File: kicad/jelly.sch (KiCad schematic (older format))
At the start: 1 part

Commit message: Add some components
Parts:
- added BT1: BATTERY, battery_custom, symbol BATTERY
- added D1, D2: LED, KiCad/LEDs.pretty:LED-5MM, symbol LED-RESCUE-bristle_bot
- added M1, M2: PAGER_MOTOR, footprints:pager_motor_custom, symbol Pager_motor
- added P1, P2, P3, P4, P5, P6, P7, P8: CONN_01X01, KiCad/Pin_Headers.pretty:Pin_Header_Straight_1x01, symbol CONN_01X01
- added Q1, Q2: 2N7000, KiCad/TO_SOT_Packages_THT.pretty:TO-92_Rugged, symbol 2N7000
- added R1, R3: 220, KiCad/Discret.pretty:R1, symbol R-RESCUE-bristle_bot
- added R2, R4: R, KiCad/Discret.pretty:R3-5, symbol R-RESCUE-bristle_bot
- added RV1: DUAL_POT, symbol DUAL_POT
- added SW1: SWITCH_INV, switch_small_custom, symbol SWITCH_INV
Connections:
- new net: BT1.1 (+), SW1.1
- new net: Q1.2 (G), R1.2, RV1.4
- new net: Q2.2 (G), R3.2, RV1.1
- new net: D2.2 (K), R4.2
- new net: D1.2 (K), R2.2
- new net GND: BT1.2 (-), Q1.1 (S), Q2.1 (S), RV1.2, RV1.5
- new net VCC: D1.1 (A), D2.1 (A), M1.1 (+), M2.1 (+), P1.1 (P1), P2.1 (P1), P7.1 (P1), P8.1 (P1), R1.1, R3.1, SW1.2
- new net Vout1: M1.2 (-), P3.1 (P1), P5.1 (P1), Q1.3 (D), R2.1
- new net Vout2: M2.2 (-), P4.1 (P1), P6.1 (P1), Q2.3 (D), R4.1

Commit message: Play with layout
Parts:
- BT1: footprint battery_custom -> (none)
- SW1: footprint switch_small_custom -> (none)
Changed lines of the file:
@@
 F 0 "BT1" H 5550 6200 50  0000 C CNN
 F 1 "BATTERY" H 5550 5810 50  0000 C CNN
-F 2 "battery_custom" H 5550 6000 60  0000 C CNN
+F 2 "" H 5550 6000 60  0000 C CNN
 F 3 "~" H 5550 6000 60  0000 C CNN
 	1    5550 6000
@@
 $EndComp
 $Comp
-L GND-RESCUE-bristle_bot #PWR3
+L GND-RESCUE-bristle_bot #PWR01
 U 1 1 57C0D38E
 P 6000 6000
-F 0 "#PWR3" H 6000 6000 30  0001 C CNN
+F 0 "#PWR01" H 6000 6000 30  0001 C CNN
 F 1 "GND" H 6000 5930 30  0001 C CNN
 F 2 "" H 6000 6000 60  0000 C CNN
@@
 $EndComp
 $Comp
-L VCC #PWR1
+L VCC #PWR02
 U 1 1 57C0D391
 P 3900 6100
-F 0 "#PWR1" H 3900 6200 30  0001 C CNN
+F 0 "#PWR02" H 3900 6200 30  0001 C CNN
 F 1 "VCC" H 3900 6200 30  0000 C CNN
 F 2 "" H 3900 6100 60  0000 C CNN
@@
 $EndComp
 $Comp
-L VCC #PWR2
+L VCC #PWR03
 U 1 1 57C0D393
 P 5300 2800
-F 0 "#PWR2" H 5300 2900 30  0001 C CNN
+F 0 "#PWR03" H 5300 2900 30  0001 C CNN
 F 1 "VCC" H 5300 2900 30  0000 C CNN
 F 2 "" H 5300 2800 60  0000 C CNN
@@
 $EndComp
 $Comp
-L VCC #PWR4
+L VCC #PWR04
 U 1 1 57C0D394
 P 6300 2550
-F 0 "#PWR4" H 6300 2650 30  0001 C CNN
+F 0 "#PWR04" H 6300 2650 30  0001 C CNN
 F 1 "VCC" H 6300 2650 30  0000 C CNN
 F 2 "" H 6300 2550 60  0000 C CNN
@@
 $EndComp
 $Comp
-L GND-RESCUE-bristle_bot #PWR5
+L GND-RESCUE-bristle_bot #PWR05
 U 1 1 57C0D395
 P 6750 3050
-F 0 "#PWR5" H 6750 3050 30  0001 C CNN
+F 0 "#PWR05" H 6750 3050 30  0001 C CNN
 F 1 "GND" H 6750 2980 30  0001 C CNN
 F 2 "" H 6750 3050 60  0000 C CNN
@@
 $EndComp
 $Comp
-L VCC #PWR9
+L VCC #PWR06
 U 1 1 57C0D397
 P 8150 2550
-F 0 "#PWR9" H 8150 2650 30  0001 C CNN
+F 0 "#PWR06" H 8150 2650 30  0001 C CNN
 F 1 "VCC" H 8150 2650 30  0000 C CNN
 F 2 "" H 8150 2550 60  0000 C CNN
@@
 $EndComp
 $Comp
-L GND-RESCUE-bristle_bot #PWR10
+L GND-RESCUE-bristle_bot #PWR07
 U 1 1 57C0D399
 P 8650 3050
-F 0 "#PWR10" H 8650 3050 30  0001 C CNN
+F 0 "#PWR07" H 8650 3050 30  0001 C CNN
 F 1 "GND" H 8650 2980 30  0001 C CNN
 F 2 "" H 8650 3050 60  0000 C CNN
@@
 $EndComp
 $Comp
-L VCC #PWR7
+L VCC #PWR08
 U 1 1 57C0D39B
 P 7150 2800
-F 0 "#PWR7" H 7150 2900 30  0001 C CNN
+F 0 "#PWR08" H 7150 2900 30  0001 C CNN
 F 1 "VCC" H 7150 2900 30  0000 C CNN
 F 2 "" H 7150 2800 60  0000 C CNN
@@
 F 0 "SW1" H 4400 6250 50  0000 C CNN
 F 1 "SWITCH_INV" H 4450 5950 50  0000 C CNN
-F 2 "switch_small_custom" H 4600 6100 60  0000 C CNN
+F 2 "" H 4600 6100 60  0000 C CNN
 F 3 "~" H 4600 6100 60  0000 C CNN
 	1    4600 6100
@@
 $EndComp
 $Comp
-L VCC #PWR13
+L VCC #PWR09
 U 1 1 57C0D3A1
 P 9500 2600
-F 0 "#PWR13" H 9500 2700 30  0001 C CNN
+F 0 "#PWR09" H 9500 2700 30  0001 C CNN
 F 1 "VCC" H 9500 2700 30  0000 C CNN
 F 2 "" H 9500 2600 60  0000 C CNN
@@
 $EndComp
 $Comp
-L VCC #PWR8
+L VCC #PWR010
 U 1 1 57C0D3A4
 P 7650 2600
-F 0 "#PWR8" H 7650 2700 30  0001 C CNN
+F 0 "#PWR010" H 7650 2700 30  0001 C CNN
 F 1 "VCC" H 7650 2700 30  0000 C CNN
 F 2 "" H 7650 2600 60  0000 C CNN
@@
 $EndComp
 $Comp
-L VCC #PWR12
+L VCC #PWR011
 U 1 1 57C0D3AE
 P 9150 4300
-F 0 "#PWR12" H 9150 4400 30  0001 C CNN
+F 0 "#PWR011" H 9150 4400 30  0001 C CNN
 F 1 "VCC" H 9150 4400 30  0000 C CNN
 F 2 "" H 9150 4300 60  0000 C CNN
@@
 $EndComp
 $Comp
-L VCC #PWR11
+L VCC #PWR012
 U 1 1 57C0D3AF
 P 9050 5150
-F 0 "#PWR11" H 9050 5250 30  0001 C CNN
+F 0 "#PWR012" H 9050 5250 30  0001 C CNN
 F 1 "VCC" H 9050 5250 30  0000 C CNN
 F 2 "" H 9050 5150 60  0000 C CNN
@@
 $EndComp
 $Comp
-L VCC #PWR15
+L VCC #PWR013
 U 1 1 57C0D3B0
 P 10700 4300
-F 0 "#PWR15" H 10700 4400 30  0001 C CNN
+F 0 "#PWR013" H 10700 4400 30  0001 C CNN
 F 1 "VCC" H 10700 4400 30  0000 C CNN
 F 2 "" H 10700 4300 60  0000 C CNN
@@
 $EndComp
 $Comp
-L VCC #PWR14
+L VCC #PWR014
 U 1 1 57C0D3B1
 P 10600 5150
-F 0 "#PWR14" H 10600 5250 30  0001 C CNN
+F 0 "#PWR014" H 10600 5250 30  0001 C CNN
 F 1 "VCC" H 10600 5250 30  0000 C CNN
 F 2 "" H 10600 5150 60  0000 C CNN
@@
 F 0 "RV1" H 7460 3860 50  0000 C CNN
 F 1 "DUAL_POT" H 7590 3250 50  0000 C CNN
-F 2 "" H 7300 3550 50  0000 C CNN
+F 2 "" H 7300 3550 50  0001 C CNN
 F 3 "" H 7300 3550 50  0000 C CNN
 	1    7300 3550
@@
 Connection ~ 9750 5150
 $Comp
-L GND #PWR6
+L GND #PWR015
 U 1 1 57C0E4F8
 P 7100 3950
-F 0 "#PWR6" H 7100 3700 50  0001 C CNN
+F 0 "#PWR015" H 7100 3700 50  0001 C CNN
 F 1 "GND" H 7100 3800 50  0000 C CNN
 F 2 "" H 7100 3950 50  0000 C CNN

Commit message: Layout some components
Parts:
- added P10, P9: CONN_01X01, footprints:hole, symbol CONN_01X01
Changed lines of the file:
@@
 F 0 "BT1" H 5550 6200 50  0000 C CNN
 F 1 "BATTERY" H 5550 5810 50  0000 C CNN
-F 2 "" H 5550 6000 60  0000 C CNN
+F 2 "" H 5550 6000 60  0001 C CNN
 F 3 "~" H 5550 6000 60  0000 C CNN
 	1    5550 6000
@@
 F 0 "SW1" H 4400 6250 50  0000 C CNN
 F 1 "SWITCH_INV" H 4450 5950 50  0000 C CNN
-F 2 "" H 4600 6100 60  0000 C CNN
+F 2 "" H 4600 6100 60  0001 C CNN
 F 3 "~" H 4600 6100 60  0000 C CNN
 	1    4600 6100
@@
 Wire Wire Line
 	7600 3300 7600 3400
+$Comp
+L CONN_01X01 P9
+U 1 1 57C22947
+P 7800 6000
+F 0 "P9" H 7800 6100 50  0000 C CNN
+F 1 "CONN_01X01" V 7900 6000 50  0000 C CNN
+F 2 "footprints:hole" H 7800 6000 50  0001 C CNN
+F 3 "" H 7800 6000 50  0000 C CNN
+	1    7800 6000
+	0    -1   -1   0
+$EndComp
+$Comp
+L CONN_01X01 P10
+U 1 1 57C229B5
+P 8300 6000
+F 0 "P10" H 8300 6100 50  0000 C CNN
+F 1 "CONN_01X01" V 8400 6000 50  0000 C CNN
+F 2 "footprints:hole" H 8300 6000 50  0001 C CNN
+F 3 "" H 8300 6000 50  0000 C CNN
+	1    8300 6000
+	0    -1   -1   0
+$EndComp
 $EndSCHEMATC

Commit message: Move things about
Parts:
- BT1: footprint (none) -> KiCad/Connectors_JST.pretty:JST_PH_S2B-PH-K_02x2.00mm_Angled
- RV1: footprint (none) -> pelrun/libKiCad/footprint/w_pth_resistors.pretty:trimmer_alps_rk12l12c0-f20-c0
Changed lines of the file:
@@
 F 0 "BT1" H 5550 6200 50  0000 C CNN
 F 1 "BATTERY" H 5550 5810 50  0000 C CNN
-F 2 "" H 5550 6000 60  0001 C CNN
+F 2 "KiCad/Connectors_JST.pretty:JST_PH_S2B-PH-K_02x2.00mm_Angled" H 5550 6000 60  0001 C CNN
 F 3 "~" H 5550 6000 60  0000 C CNN
 	1    5550 6000
@@
 F 0 "RV1" H 7460 3860 50  0000 C CNN
 F 1 "DUAL_POT" H 7590 3250 50  0000 C CNN
-F 2 "" H 7300 3550 50  0001 C CNN
+F 2 "pelrun/libKiCad/footprint/w_pth_resistors.pretty:trimmer_alps_rk12l12c0-f20-c0" H 7300 3550 50  0001 C CNN
 F 3 "" H 7300 3550 50  0000 C CNN
 	1    7300 3550

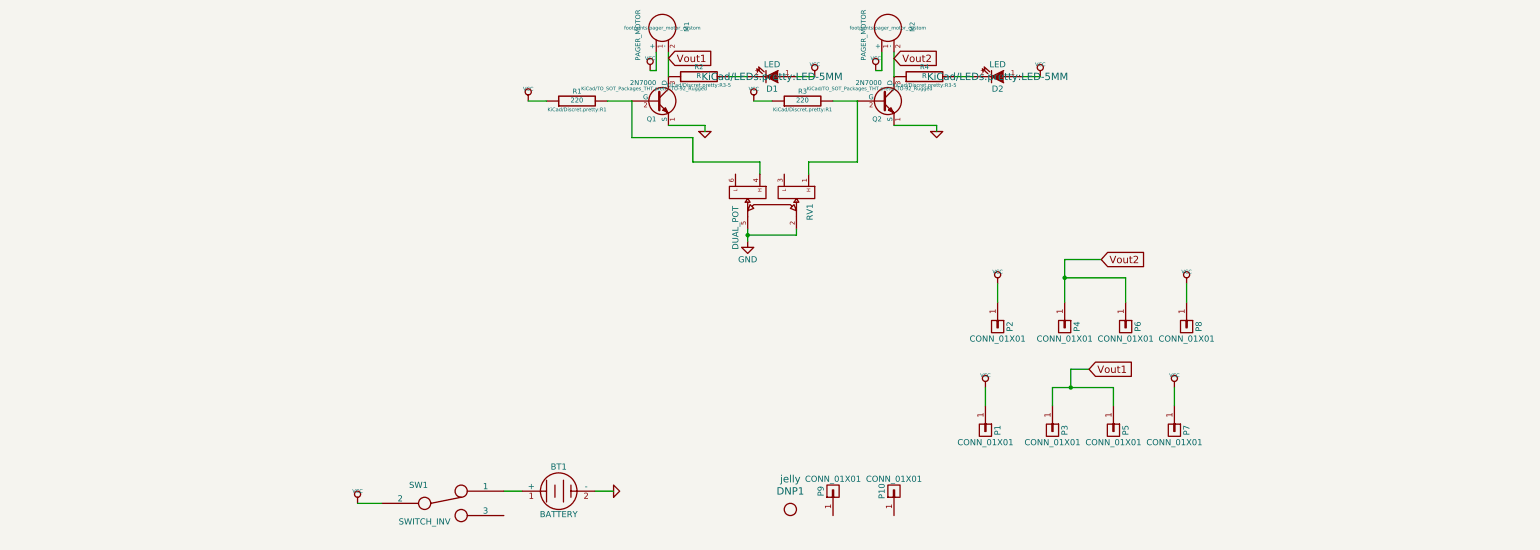
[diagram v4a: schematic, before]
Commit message: Add LDR silkscreen image
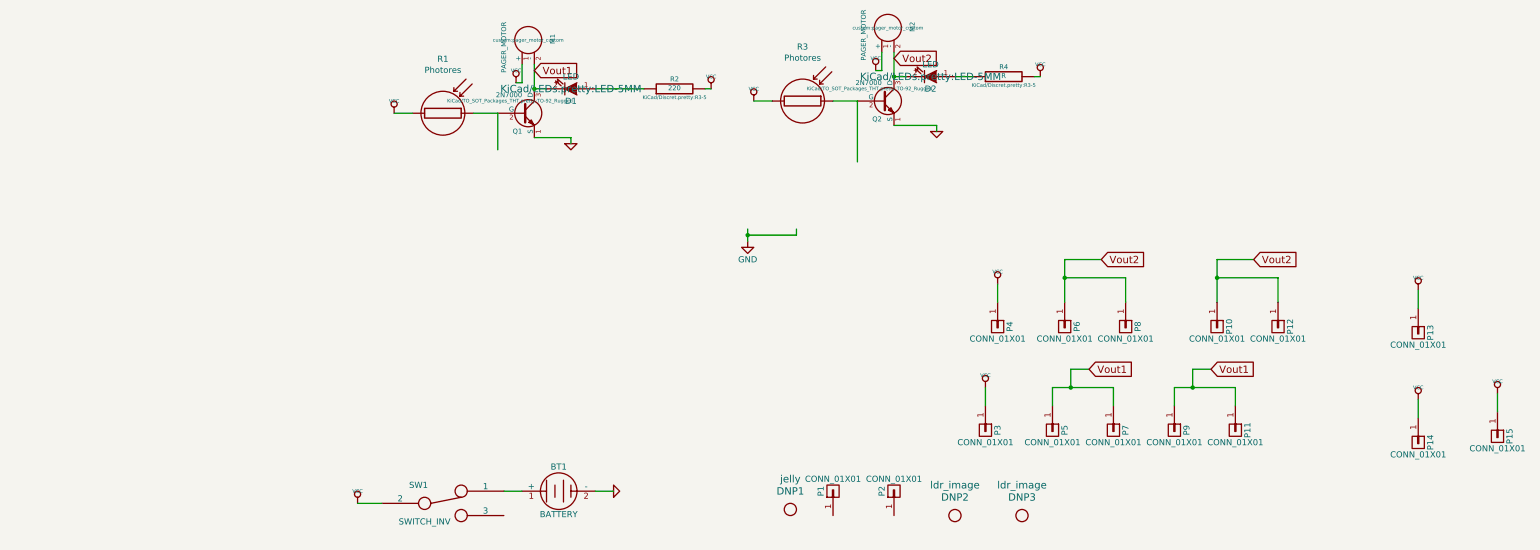
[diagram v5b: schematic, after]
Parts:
- removed R1, R3: 220, KiCad/Discret.pretty:R1, symbol R-RESCUE-bristle_bot
- removed RV1: DUAL_POT, pelrun/libKiCad/footprint/w_pth_resistors.pretty:trimmer_alps_rk12l12c0-f20-c0, symbol DUAL_POT
- added DNP2, DNP3: ldr_image, custom:jelly, symbol placeholder
- added P10, P11, P12, P15, P9: CONN_01X01, custom:hole2, symbol CONN_01X01
- added R1, R3: Photores, custom:ldr, symbol Photores
- DNP1: footprint footprints:jelly -> custom:jelly
- M1, M2: footprint footprints:pager_motor_custom -> custom:pager_motor_custom
- P1: renamed from P9; footprint footprints:hole -> custom:hole
- P13: renamed from P8; footprint KiCad/Pin_Headers.pretty:Pin_Header_Straight_1x01 -> custom:hole2
- P14: renamed from P7; footprint KiCad/Pin_Headers.pretty:Pin_Header_Straight_1x01 -> custom:hole2
- P2: renamed from P10; footprint footprints:hole -> custom:hole
- P3: renamed from P1; footprint KiCad/Pin_Headers.pretty:Pin_Header_Straight_1x01 -> custom:hole2
- P4: renamed from P2; footprint KiCad/Pin_Headers.pretty:Pin_Header_Straight_1x01 -> custom:hole2
- P5: renamed from P3; footprint KiCad/Pin_Headers.pretty:Pin_Header_Straight_1x01 -> custom:hole2
- P6: renamed from P4; footprint KiCad/Pin_Headers.pretty:Pin_Header_Straight_1x01 -> custom:hole2
- P7: renamed from P5; footprint KiCad/Pin_Headers.pretty:Pin_Header_Straight_1x01 -> custom:hole2
- P8: renamed from P6; footprint KiCad/Pin_Headers.pretty:Pin_Header_Straight_1x01 -> custom:hole2
- R2: value R -> 220
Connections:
- wire segments 45 -> 51
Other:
- moved on the sheet: D1, D2, M1, P13, P14, Q1, R2, R4

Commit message: Re-arrange connector holes
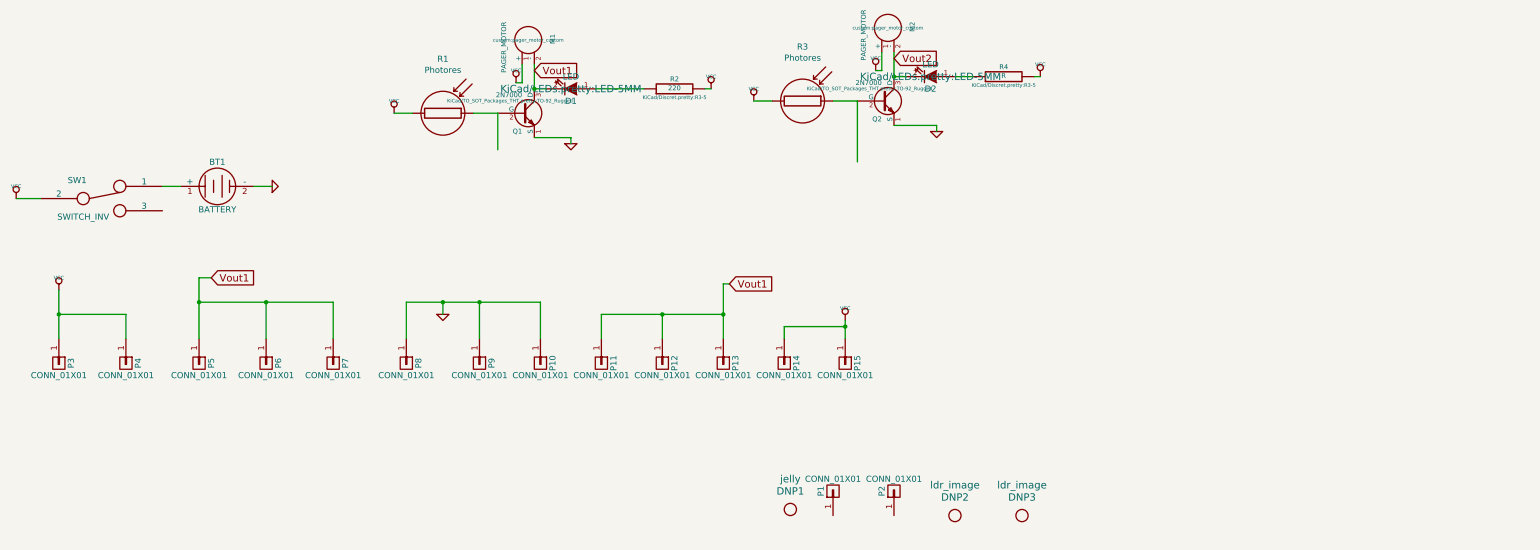
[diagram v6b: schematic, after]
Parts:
- DNP2, DNP3: footprint custom:jelly -> custom:ldr_image
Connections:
- wire segments 51 -> 46
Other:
- moved on the sheet: BT1, P10, P11, P12, P13, P14, P15, P3, P4, P5, P6, P7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

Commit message: Play around with some routing
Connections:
- wire segments 46 -> 48
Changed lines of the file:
@@
 Text GLabel 8300 2450 2    60   Input ~ 0
 Vout2
-Wire Wire Line
-	5050 2900 5050 3200
-Wire Wire Line
-	3050 3500 3200 3500
-Wire Wire Line
-	5350 2500 5350 2700
-Wire Wire Line
-	2450 3500 2300 3500
-Wire Wire Line
-	5050 2900 4850 2900
-Wire Wire Line
-	4350 2900 4200 2900
-Wire Wire Line
-	5250 2500 5250 2650
-Wire Wire Line
-	5250 2650 5200 2650
-Wire Wire Line
-	5350 3100 5650 3100
-Wire Wire Line
-	5650 3100 5650 3150
-Wire Wire Line
-	8300 2600 8300 2400
-Wire Wire Line
-	8200 2400 8200 2550
-Wire Wire Line
-	8200 2550 8150 2550
-Wire Wire Line
-	8000 2800 7800 2800
-Wire Wire Line
-	7300 2800 7150 2800
-Wire Wire Line
-	8000 2800 8000 3300
-Wire Wire Line
-	8300 3000 8650 3000
-Wire Wire Line
-	8650 3000 8650 3050
-Wire Wire Line
-	1300 3600 1100 3600
-Wire Wire Line
-	5850 2700 6250 2700
-Wire Wire Line
-	8950 2600 8800 2600
-Wire Wire Line
-	1450 4350 1450 4750
 $Comp
 L CONN_01X01 P1
@@
 	1    0    0    -1
 $EndComp
-Wire Wire Line
-	7900 4600 7900 4750
-Wire Wire Line
-	9450 2600 9500 2600
-Wire Wire Line
-	8400 2600 8300 2600
-Connection ~ 8300 2600
-Wire Wire Line
-	5350 2700 5450 2700
-Connection ~ 5350 2700
-Wire Wire Line
-	6750 2700 6800 2700
 $Comp
 L Photores R1
@@
 	1    0    0    -1
 $EndComp
-Wire Wire Line
-	1450 4550 2000 4550
-Wire Wire Line
-	2000 4550 2000 4750
-Connection ~ 1450 4550
-Wire Wire Line
-	7400 4750 7400 4650
-Wire Wire Line
-	7400 4650 7900 4650
-Connection ~ 7900 4650
 Text GLabel 2700 4250 2    60   Input ~ 0
 Vout1
-Wire Wire Line
-	2700 4250 2600 4250
-Wire Wire Line
-	2600 4250 2600 4750
-Text GLabel 6950 4300 2    60   Input ~ 0
-Vout1
-Wire Wire Line
-	2600 4450 3700 4450
-Connection ~ 2600 4450
-Wire Wire Line
-	3150 4450 3150 4750
-Connection ~ 3150 4450
-Wire Wire Line
-	6900 4750 6900 4300
-Wire Wire Line
-	6900 4300 6950 4300
-Wire Wire Line
-	6400 4750 6400 4550
-Wire Wire Line
-	5900 4550 6900 4550
-Connection ~ 6900 4550
-Wire Wire Line
-	5900 4750 5900 4550
-Connection ~ 6400 4550
-Wire Wire Line
-	3700 4450 3700 4750
+Text GLabel 6450 4300 2    60   Input ~ 0
+Vout2
 $Comp
 L GND-RESCUE-bristle_bot #PWR?
@@
 $EndComp
 Wire Wire Line
+	5050 2900 5050 3200
+Wire Wire Line
+	3050 3500 3200 3500
+Wire Wire Line
+	5350 2500 5350 2700
+Wire Wire Line
+	2450 3500 2300 3500
+Wire Wire Line
+	5050 2900 4850 2900
+Wire Wire Line
+	4350 2900 4200 2900
+Wire Wire Line
+	5250 2500 5250 2650
+Wire Wire Line
+	5250 2650 5200 2650
+Wire Wire Line
+	5350 3100 5650 3100
+Wire Wire Line
+	5650 3100 5650 3150
+Wire Wire Line
+	8300 2600 8300 2400
+Wire Wire Line
+	8200 2400 8200 2550
+Wire Wire Line
+	8200 2550 8150 2550
+Wire Wire Line
+	8000 2800 7800 2800
+Wire Wire Line
+	7300 2800 7150 2800
+Wire Wire Line
+	8000 2800 8000 3300
+Wire Wire Line
+	8300 3000 8650 3000
+Wire Wire Line
+	8650 3000 8650 3050
+Wire Wire Line
+	1300 3600 1100 3600
+Wire Wire Line
+	5850 2700 6250 2700
+Wire Wire Line
+	8950 2600 8800 2600
+Wire Wire Line
+	1450 4350 1450 4750
+Wire Wire Line
+	7900 4600 7900 4750
+Wire Wire Line
+	9450 2600 9500 2600
+Wire Wire Line
+	8400 2600 8300 2600
+Connection ~ 8300 2600
+Wire Wire Line
+	5350 2700 5450 2700
+Connection ~ 5350 2700
+Wire Wire Line
+	6750 2700 6800 2700
+Wire Wire Line
+	1450 4550 2000 4550
+Wire Wire Line
+	2000 4550 2000 4750
+Connection ~ 1450 4550
+Wire Wire Line
+	7400 4750 7400 4650
+Wire Wire Line
+	6900 4650 7900 4650
+Connection ~ 7900 4650
+Wire Wire Line
+	2700 4250 2600 4250
+Wire Wire Line
+	2600 4250 2600 4750
+Wire Wire Line
+	2600 4450 3700 4450
+Connection ~ 2600 4450
+Wire Wire Line
+	3150 4450 3150 4750
+Connection ~ 3150 4450
+Wire Wire Line
+	6400 4300 6400 4750
+Wire Wire Line
+	6400 4300 6450 4300
+Wire Wire Line
+	5400 4550 6400 4550
+Wire Wire Line
+	5900 4750 5900 4550
+Connection ~ 6400 4550
+Wire Wire Line
+	3700 4450 3700 4750
+Wire Wire Line
 	4300 4450 4300 4750
-Wire Wire Line
-	4300 4450 5400 4450
 Wire Wire Line
 	4600 4450 4600 4550
@@
 	4900 4450 4900 4750
 Connection ~ 4600 4450
-Wire Wire Line
-	5400 4450 5400 4750
 Connection ~ 4900 4450
+Wire Wire Line
+	4300 4450 4900 4450
+Wire Wire Line
+	5400 4750 5400 4550
+Connection ~ 5900 4550
+Wire Wire Line
+	6900 4750 6900 4650
+Connection ~ 7400 4650
+$Comp
+L VCC #PWR?
+U 1 1 57C3486C
+P 8450 6350
+F 0 "#PWR?" H 8450 6450 30  0001 C CNN
+F 1 "VCC" H 8450 6450 30  0000 C CNN
+F 2 "" H 8450 6350 60  0000 C CNN
+F 3 "" H 8450 6350 60  0000 C CNN
+	1    8450 6350
+	0    1    1    0
+$EndComp
+Wire Wire Line
+	8300 6200 8300 6350
+Wire Wire Line
+	8300 6350 8450 6350
 $EndSCHEMATC

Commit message: Switch to CR2450 battery holder
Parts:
- BT1: footprint KiCad/Connectors_JST.pretty:JST_PH_S2B-PH-K_02x2.00mm_Angled -> custom:cr2450_holder
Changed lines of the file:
@@
 F 0 "BT1" H 2750 3700 50  0000 C CNN
 F 1 "BATTERY" H 2750 3310 50  0000 C CNN
-F 2 "KiCad/Connectors_JST.pretty:JST_PH_S2B-PH-K_02x2.00mm_Angled" H 2750 3500 60  0001 C CNN
+F 2 "custom:cr2450_holder" H 2750 3500 60  0001 C CNN
 F 3 "~" H 2750 3500 60  0000 C CNN
 	1    2750 3500
@@
 $EndComp
 $Comp
-L VCC #PWR013
+L VCC #PWR011
 U 1 1 57C0D3B0
 P 1450 4350
-F 0 "#PWR013" H 1450 4450 30  0001 C CNN
+F 0 "#PWR011" H 1450 4450 30  0001 C CNN
 F 1 "VCC" H 1450 4450 30  0000 C CNN
 F 2 "" H 1450 4350 60  0000 C CNN
@@
 $EndComp
 $Comp
-L VCC #PWR016
+L VCC #PWR012
 U 1 1 57C309E3
 P 7900 4600
-F 0 "#PWR016" H 7900 4700 30  0001 C CNN
+F 0 "#PWR012" H 7900 4700 30  0001 C CNN
 F 1 "VCC" H 7900 4700 30  0000 C CNN
 F 2 "" H 7900 4600 60  0000 C CNN
@@
 Vout2
 $Comp
-L GND-RESCUE-bristle_bot #PWR?
+L GND-RESCUE-bristle_bot #PWR013
 U 1 1 57C36163
 P 4600 4550
-F 0 "#PWR?" H 4600 4550 30  0001 C CNN
+F 0 "#PWR013" H 4600 4550 30  0001 C CNN
 F 1 "GND" H 4600 4480 30  0001 C CNN
 F 2 "" H 4600 4550 60  0000 C CNN
@@
 Connection ~ 7400 4650
 $Comp
-L VCC #PWR?
+L VCC #PWR014
 U 1 1 57C3486C
 P 8450 6350
-F 0 "#PWR?" H 8450 6450 30  0001 C CNN
+F 0 "#PWR014" H 8450 6450 30  0001 C CNN
 F 1 "VCC" H 8450 6450 30  0000 C CNN
 F 2 "" H 8450 6350 60  0000 C CNN
